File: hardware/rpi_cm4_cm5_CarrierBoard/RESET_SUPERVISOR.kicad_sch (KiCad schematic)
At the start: 21 parts, among them Q1 2N7002, Q2 2N7002, Q3 2N7002, U1 STM6710DWB6F, U2 SN74LVC1G125DBVR, U3 SN74LVC1G125DBVR

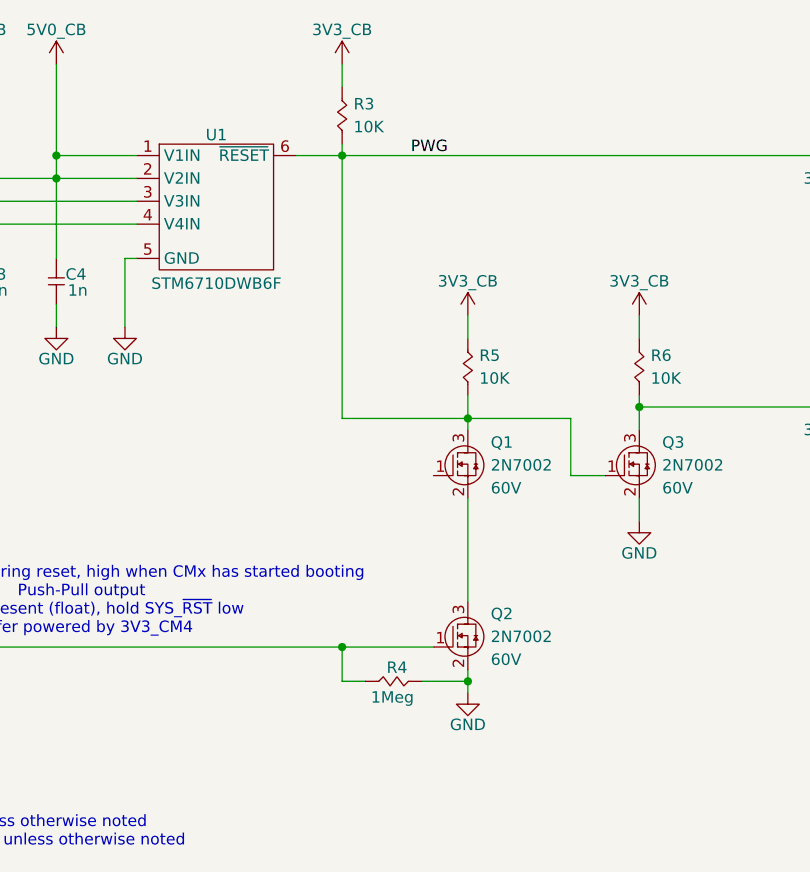
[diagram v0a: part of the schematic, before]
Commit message: Add power-up and power kill sequences Modify schematics to add net classes for DiffPairs
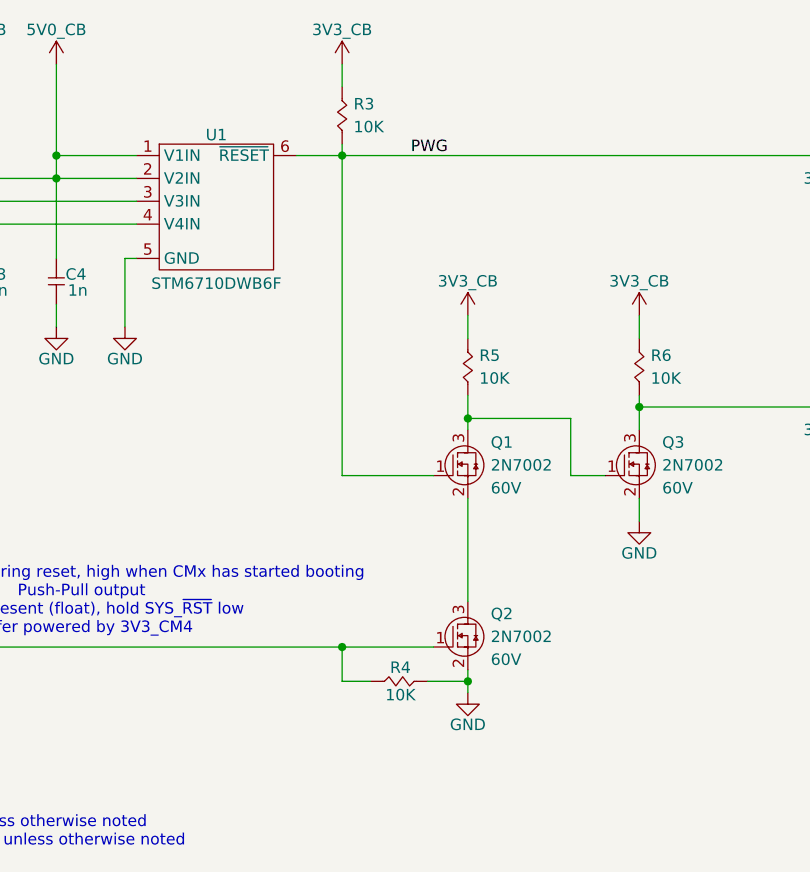
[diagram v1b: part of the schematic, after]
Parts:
- removed R4: 1Meg, footprint:RES_0402, symbol KicadCompDb:Resistors/RES_SMT_00006
- added R4: 10K, footprint:RES_0402, symbol KicadCompDb:Resistors/RES_SMT_00013
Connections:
- net EXT_~{RST}: now also R4.2
- net GND: now also R4.1
- net PWG: now also Q1.1 (G); no longer Q1.3 (D), Q3.1 (G), R5.1
- new net: Q1.3 (D), Q3.1 (G), R5.1
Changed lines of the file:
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@@
 	(wire
 		(pts
+			(xy 126.365 97.79) (xy 136.525 97.79)
+		)
+		(stroke
+			(width 0)
+			(type default)
+		)
+	)
+	(wire
+		(pts
 			(xy 159.385 88.9) (xy 159.385 90.17)
 		)
@@
 	(wire
 		(pts
-			(xy 126.365 120.65) (xy 128.905 120.65)
+			(xy 126.365 120.65) (xy 129.54 120.65)
 		)
 		(stroke
@@
 	(wire
 		(pts
+			(xy 126.365 62.23) (xy 126.365 97.79)
+		)
+		(stroke
+			(width 0)
+			(type default)
+		)
+	)
+	(wire
+		(pts
 			(xy 140.335 88.9) (xy 140.335 91.44)
 		)
@@
 	(wire
 		(pts
-			(xy 126.365 62.23) (xy 126.365 91.44)
-		)
-		(stroke
-			(width 0)
-			(type default)
-		)
-	)
-	(wire
-		(pts
 			(xy 140.335 91.44) (xy 140.335 92.71)
 		)
@@
 	(wire
 		(pts
-			(xy 135.255 120.65) (xy 140.335 120.65)
+			(xy 135.89 120.65) (xy 140.335 120.65)
 		)
 		(stroke
@@
 	(wire
 		(pts
-			(xy 140.335 91.44) (xy 126.365 91.44)
-		)
-		(stroke
-			(width 0)
-			(type default)
-		)
-	)
-	(wire
-		(pts
 			(xy 85.725 52.07) (xy 85.725 64.77)
 		)
@@
 	(symbol
 		(lib_id "KicadCompDb:Resistors/RES_SMT_00013")
+		(at 134.62 120.65 180)
+		(unit 1)
+		(exclude_from_sim no)
+		(in_bom yes)
+		(on_board yes)
+		(dnp no)
+		(property "Reference" "R4"
+			(at 132.842 119.126 0)
+			(effects
+				(font
+					(size 1.27 1.27)
+				)
+			)
+		)
+		(property "Value" "10K"
+			(at 132.842 122.174 0)
+			(effects
+				(font
+					(size 1.27 1.27)
+				)
+			)
+		)
+		(property "Footprint" "footprint:RES_0402"
+			(at 134.112 98.552 0)
+			(effects
+				(font
+					(size 1.27 1.27)
+				)
+				(hide yes)
+			)
+		)
+		(property "Datasheet" "https://www.yageogroup.com/content/datasheet/asset/file/PYU-RC_GROUP_51_ROHS_L"
+			(at 134.62 120.65 0)
+			(effects
+				(font
+					(size 1.27 1.27)
+				)
+				(hide yes)
+			)
+		)
+		(property "Description" "RES 10K OHM 1% 1/16W 0402"
+			(at 132.842 110.744 0)
+			(effects
+				(font
+					(size 1.27 1.27)
+				)
+				(hide yes)
+			)
+		)
+		(property "Tolerance" "1%"
+			(at 134.366 100.33 0)
+			(effects
+				(font
+					(size 1.27 1.27)
+				)
+				(hide yes)
+			)
+		)
+		(property "Power" "1/16W"
+			(at 134.366 106.426 0)
+			(effects
+				(font
+					(size 1.27 1.27)
+				)
+				(hide yes)
+			)
+		)
+		(property "Package" "0402"
+			(at 134.62 104.394 0)
+			(effects
+				(font
+					(size 1.27 1.27)
+				)
+				(hide yes)
+			)
+		)
+		(property "Manufacturer" "YAGEO"
+			(at 134.366 102.362 0)
+			(effects
+				(font
+					(size 1.27 1.27)
+				)
+				(hide yes)
+			)
+		)
+		(property "Manufacturer Part Number" "RC0402FR-0710KL"
+			(at 134.366 112.776 0)
+			(effects
+				(font
+					(size 1.27 1.27)
+				)
+				(hide yes)
+			)
+		)
+		(property "Distributor" "DigiKey"
+			(at 134.62 114.808 0)
+			(effects
+				(font
+					(size 1.27 1.27)
+				)
+				(hide yes)
+			)
+		)
+		(property "Distributor Part Number" "311-10.0KLRCT-ND"
+			(at 133.858 108.458 0)
+			(effects
+				(font
+					(size 1.27 1.27)
+				)
+				(hide yes)
+			)
+		)
+		(property "Temperature Coefficient" "±100ppm/°C"
+			(at 134.62 120.65 0)
+			(effects
+				(font
+					(size 1.27 1.27)
+				)
+				(hide yes)
+			)
+		)
+		(property "Operating Temperature" "-55°C ~ 155°C"
+			(at 133.858 96.266 0)
+			(effects
+				(font
+					(size 1.27 1.27)
+				)
+				(hide yes)
+			)
+		)
+		(property "Type" "RES SMT"
+			(at 134.62 120.65 0)
+			(show_name yes)
+			(effects
+				(font
+					(size 1.27 1.27)
+				)
+				(hide yes)
+			)
+		)
+		(property "Dimensions" "1.00mm x 0.50mm"
+			(at 134.62 120.65 0)
+			(show_name yes)
+			(effects
+				(font
+					(size 1.27 1.27)
+				)
+				(hide yes)
+			)
+		)
+		(pin "1"
+		)
+		(pin "2"
+		)
+		(instances
+			(project "rpi_cm4_cm5_CarrierBoard"
+				(path "/7dcdf741-90ca-4333-848c-806f4d64158e/9c05f41d-8810-41e2-a7f9-3345c9f4f612"
+					(reference "R4")
+					(unit 1)
+				)
+			)
+		)
+	)
+	(symbol
+		(lib_id "KicadCompDb:Resistors/RES_SMT_00013")
 		(at 126.365 59.69 90)
 		(unit 1)
@@
 					(unit 1)
 				)
-			)
-		)
-	)
-	(symbol
-		(lib_id "KicadCompDb:Resistors/RES_SMT_00006")
-		(at 130.175 120.65 0)
-		(unit 1)
-		(exclude_from_sim no)
-		(in_bom yes)
-		(on_board yes)
-		(dnp no)
-		(property "Reference" "R4"
-			(at 132.461 119.126 0)
-			(effects
-				(font
-					(size 1.27 1.27)
-				)
-			)
-		)
-		(property "Value" "1Meg"
-			(at 131.953 122.428 0)
-			(effects
-				(font
-					(size 1.27 1.27)
-				)
-			)
-		)
-		(property "Footprint" "footprint:RES_0402"
-			(at 130.683 142.748 0)
-			(effects
-				(font
-					(size 1.27 1.27)
-				)
-				(hide yes)
-			)
-		)
-		(property "Datasheet" "https://www.yageogroup.com/content/datasheet/asset/file/PYU-RC_GROUP_51_ROHS_L"
-			(at 130.175 120.65 0)
-			(effects
-				(font
-					(size 1.27 1.27)
-				)
-				(hide yes)
-			)
-		)
-		(property "Description" "RES 1M OHM 1% 1/16W 0402"
-			(at 131.953 130.556 0)
-			(effects
-				(font
-					(size 1.27 1.27)
-				)
-				(hide yes)
-			)
-		)
-		(property "Tolerance" "1%"
-			(at 130.429 140.97 0)
-			(effects
-				(font
-					(size 1.27 1.27)
-				)
-				(hide yes)
-			)
-		)
-		(property "Power" "1/16W"
-			(at 130.429 134.874 0)
-			(effects
-				(font
-					(size 1.27 1.27)
-				)
-				(hide yes)
-			)
-		)
-		(property "Package" "0402"
-			(at 130.175 136.906 0)
-			(effects
-				(font
-					(size 1.27 1.27)
-				)
-				(hide yes)
-			)
-		)
-		(property "Manufacturer" "YAGEO"
-			(at 130.429 138.938 0)
-			(effects
-				(font
-					(size 1.27 1.27)
-				)
-				(hide yes)
-			)
-		)
-		(property "Manufacturer Part Number" "RC0402FR-131ML"
-			(at 130.429 128.524 0)
-			(effects
-				(font
-					(size 1.27 1.27)
-				)
-				(hide yes)
-			)
-		)
-		(property "Distributor" "DigiKey"
-			(at 130.175 126.492 0)
-			(effects
-				(font
-					(size 1.27 1.27)
-				)
-				(hide yes)
-			)
-		)
-		(property "Distributor Part Number" "13-RC0402FR-131MLCT-ND"
-			(at 130.937 132.842 0)
-			(effects
-				(font
-					(size 1.27 1.27)
-				)
-				(hide yes)
-			)
-		)
-		(property "Temperature Coefficient" "±100ppm/°C"
-			(at 130.175 120.65 0)
-			(effects
-				(font
-					(size 1.27 1.27)
-				)
-				(hide yes)
-			)
-		)
-		(property "Operating Temperature" "-55°C ~ 155°C"
-			(at 130.937 145.034 0)
-			(effects
-				(font
-					(size 1.27 1.27)
-				)
-				(hide yes)
-			)
-		)
-		(property "Type" "RES SMT"
-			(at 130.175 120.65 0)
-			(show_name yes)
-			(effects
-				(font
-					(size 1.27 1.27)
-				)
-				(hide yes)
-			)
-		)
-		(property "Dimensions" "1.00mm x 0.50mm"
-			(at 130.175 120.65 0)
-			(show_name yes)
-			(effects
-				(font
-					(size 1.27 1.27)
-				)
-				(hide yes)
-			)
-		)
-		(pin "1"
-		)
-		(pin "2"
-		)
-		(instances
-			(project "rpi_cm4_cm5_CarrierBoard"
-				(path "/7dcdf741-90ca-4333-848c-806f4d64158e/9c05f41d-8810-41e2-a7f9-3345c9f4f612"
-					(reference "R4")
-					(unit 1)
-				)

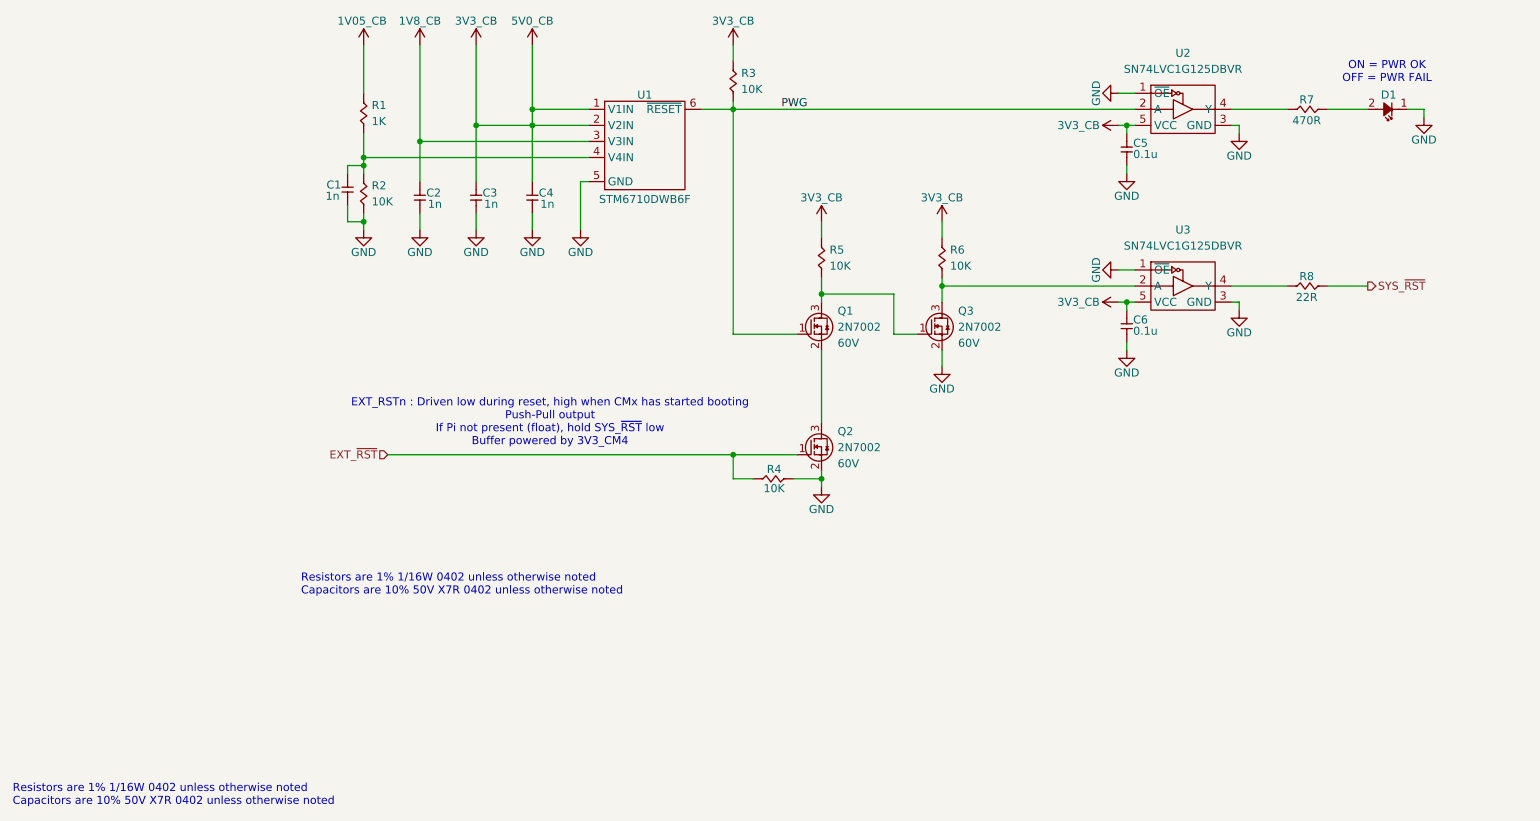
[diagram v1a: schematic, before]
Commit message: Preliminary completion of RPI CMx schematics Cleaned up hierarchical root page
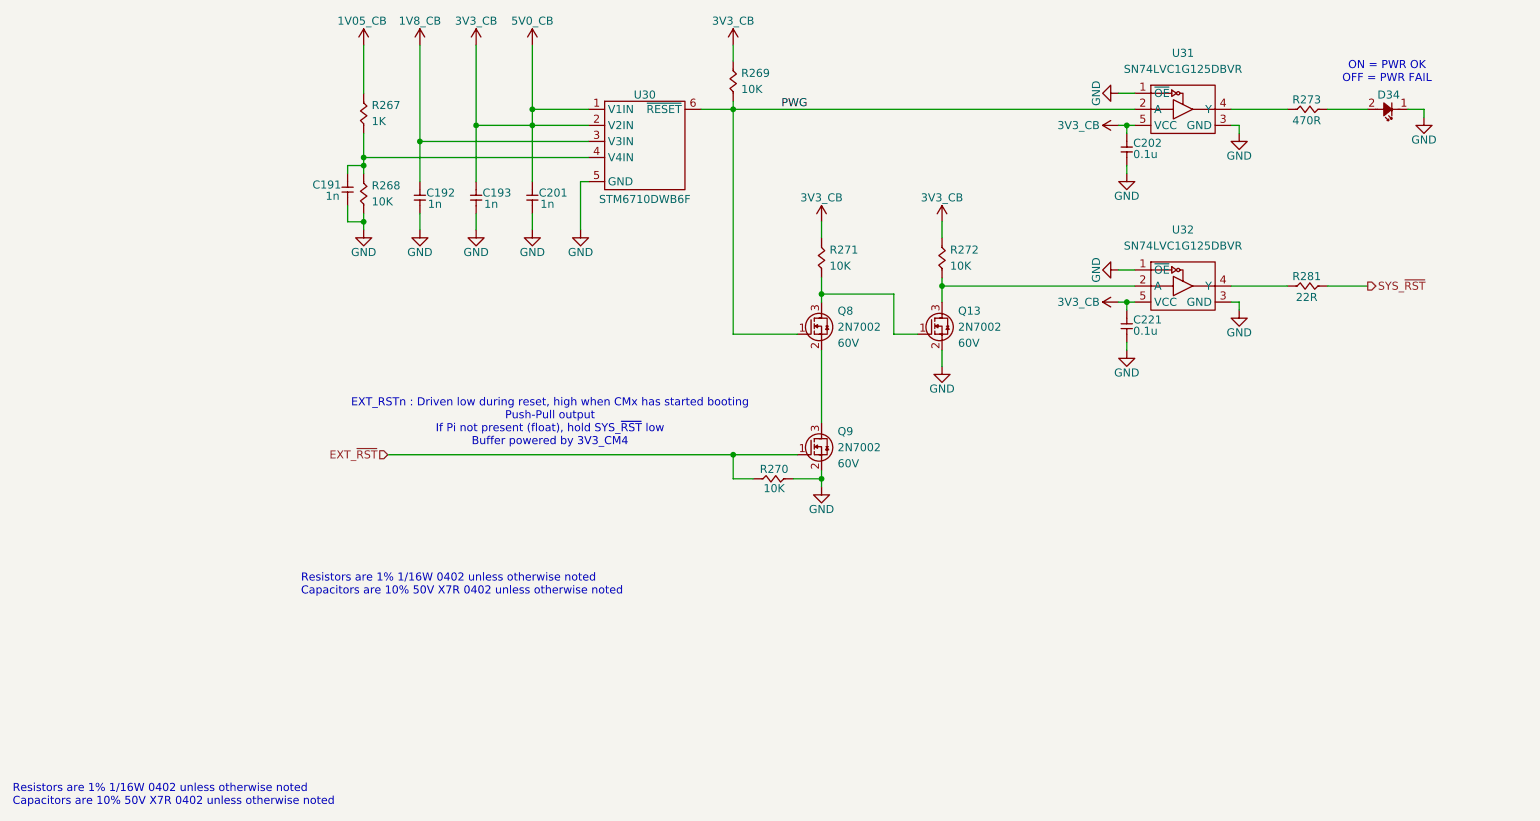
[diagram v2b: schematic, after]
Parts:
- renumbered C1 to C191, C2 to C192, C3 to C193, C4 to C201, C5 to C202, C6 to C221, D1 to D34, Q3 to Q13, Q1 to Q8, Q2 to Q9, R1 to R267, R2 to R268, R3 to R269, R4 to R270, R5 to R271, R6 to R272, R7 to R273, R8 to R281, U1 to U30, U2 to U31, U3 to U32

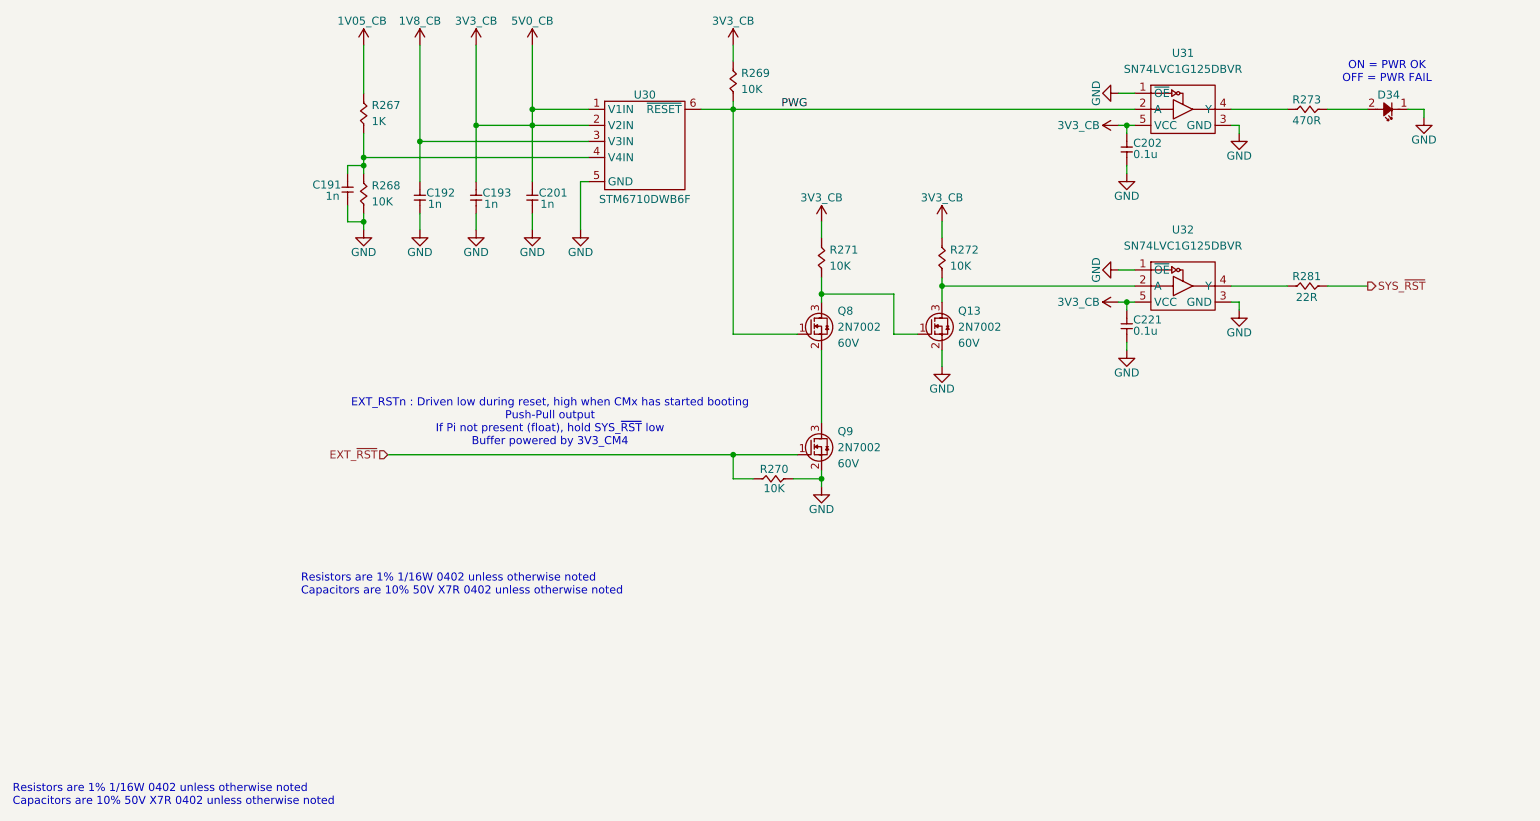
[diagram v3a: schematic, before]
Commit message: Added power input protection & filter Added dedicated QWIIC connector on RPI CMx I2C6 bus Adjusted power table and PinMux Updated schematics accordingly
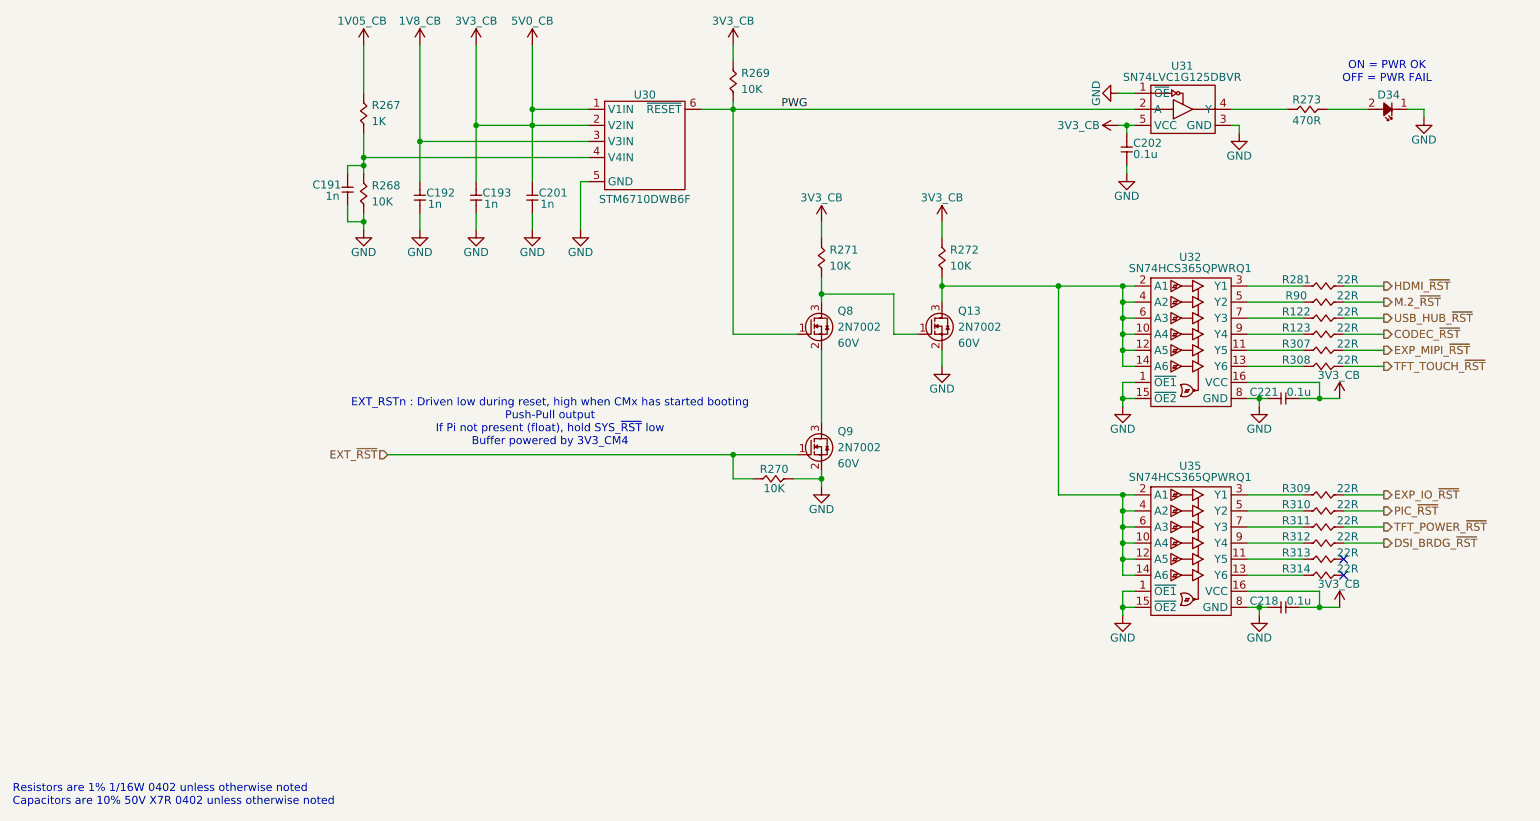
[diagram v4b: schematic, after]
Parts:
- removed U32: SN74LVC1G125DBVR, footprint:SOT-23-5, symbol KicadCompDb:Logic/LOGIC_00001
- added C218: 0.1u, footprint:CAP_NONPOL_0402, symbol KicadCompDb:Capacitors/CAP_CER_SMT_00001
- added R122, R123, R307, R308, R309, R310, R311, R312, R313, R314, R90: 22R, footprint:RES_0402, symbol KicadCompDb:Resistors/RES_SMT_00015
- added U32, U35: SN74HCS365QPWRQ1, footprint:TSSOP-16-5.8mm, symbol KicadCompDb:Logic/LOGIC_00006
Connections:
- net 3V3_CB: now also C221.1, C218.1, U32.16 (VCC), U35.16 (VCC); no longer C221.2
- net GND: now also C221.2, C218.2, U32.1 (~{OE1}), U32.15 (~{OE2}), U32.8 (GND), U35.1 (~{OE1}), U35.15 (~{OE2}), U35.8 (GND); no longer C221.1
- net at Q13.3 (D), R272.1: now also U32.10 (A4), U32.12 (A5), U32.14 (A6), U32.2 (A1), U32.4 (A2), U32.6 (A3), U35.10 (A4), U35.12 (A5), U35.14 (A6), U35.2 (A1), U35.4 (A2), U35.6 (A3)
- net at R281.1: now also U32.3 (Y1)
- net SYS_~{RST} renamed HDMI_~{RST}
- new net: R307.1, U32.11 (Y5)
- new net: R308.1, U32.13 (Y6)
- new net: R90.1, U32.5 (Y2)
- new net: R122.1, U32.7 (Y3)
- new net: R123.1, U32.9 (Y4)
- new net: R309.1, U35.3 (Y1)
- new net: R313.1, U35.11 (Y5)
- new net: R314.1, U35.13 (Y6)
- new net: R310.1, U35.5 (Y2)
- new net: R311.1, U35.7 (Y3)
- new net: R312.1, U35.9 (Y4)
- new net CODEC_~{RST}: R123.2
- new net DSI_BRDG_~{RST}: R312.2
- new net EXP_IO_~{RST}: R309.2
- new net EXP_MIPI_~{RST}: R307.2
- new net M.2_~{RST}: R90.2
- new net PIC_~{RST}: R310.2
- new net TFT_POWER_~{RST}: R311.2
- new net TFT_TOUCH_~{RST}: R308.2
- new net USB_HUB_~{RST}: R122.2
- no-connect marks 0 -> 2
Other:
- moved on the sheet: C221, R281
